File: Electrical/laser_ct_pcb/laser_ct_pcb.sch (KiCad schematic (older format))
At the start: 3 parts

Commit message: End of E07.
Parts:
- added Q? (x9): Q_Photo_NPN, symbol Device:Q_Photo_NPN
- added R? (x9): 1 kOhm, symbol Device:R_US
- added U? (x2): MCP3008, symbol Analog_ADC:MCP3008
- R?: value 10 kOhm -> 1 kOhm
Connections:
- net +5V: now also A?.27 (+5V), R?.1, R?.1, R?.1, R?.1, R?.1, R?.1, R?.1, R?.1, R?.1, U?.15 (Vref), U?.15 (Vref), U?.16 (Vdd), U?.16 (Vdd)
- net GND: now also A?.29 (GND), A?.4 (GND), Q?.2 (E), Q?.2 (E), Q?.2 (E), Q?.2 (E), Q?.2 (E), Q?.2 (E), Q?.2 (E), Q?.2 (E), Q?.2 (E), U?.14 (AGND), U?.14 (AGND), U?.9 (DGND), U?.9 (DGND)
- net at A?.12 (D9): now also U?.10 (~CS~/SHDN)
- net at A?.13 (D10): now also U?.10 (~CS~/SHDN)
- net at A?.14 (D11): now also U?.11 (Din), U?.11 (Din)
- net at A?.15 (D12): now also U?.12 (Dout), U?.12 (Dout)
- net at A?.16 (D13): now also U?.13 (CLK), U?.13 (CLK)
- new net: Q?.1 (C), R?.2 (x9)
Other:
- moved on the sheet: A?, Q?, R?

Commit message: End of Episode 08.
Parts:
- removed Q? (x10): Q_Photo_NPN, symbol Device:Q_Photo_NPN
- removed R? (x10): 1 kOhm, symbol Device:R_US

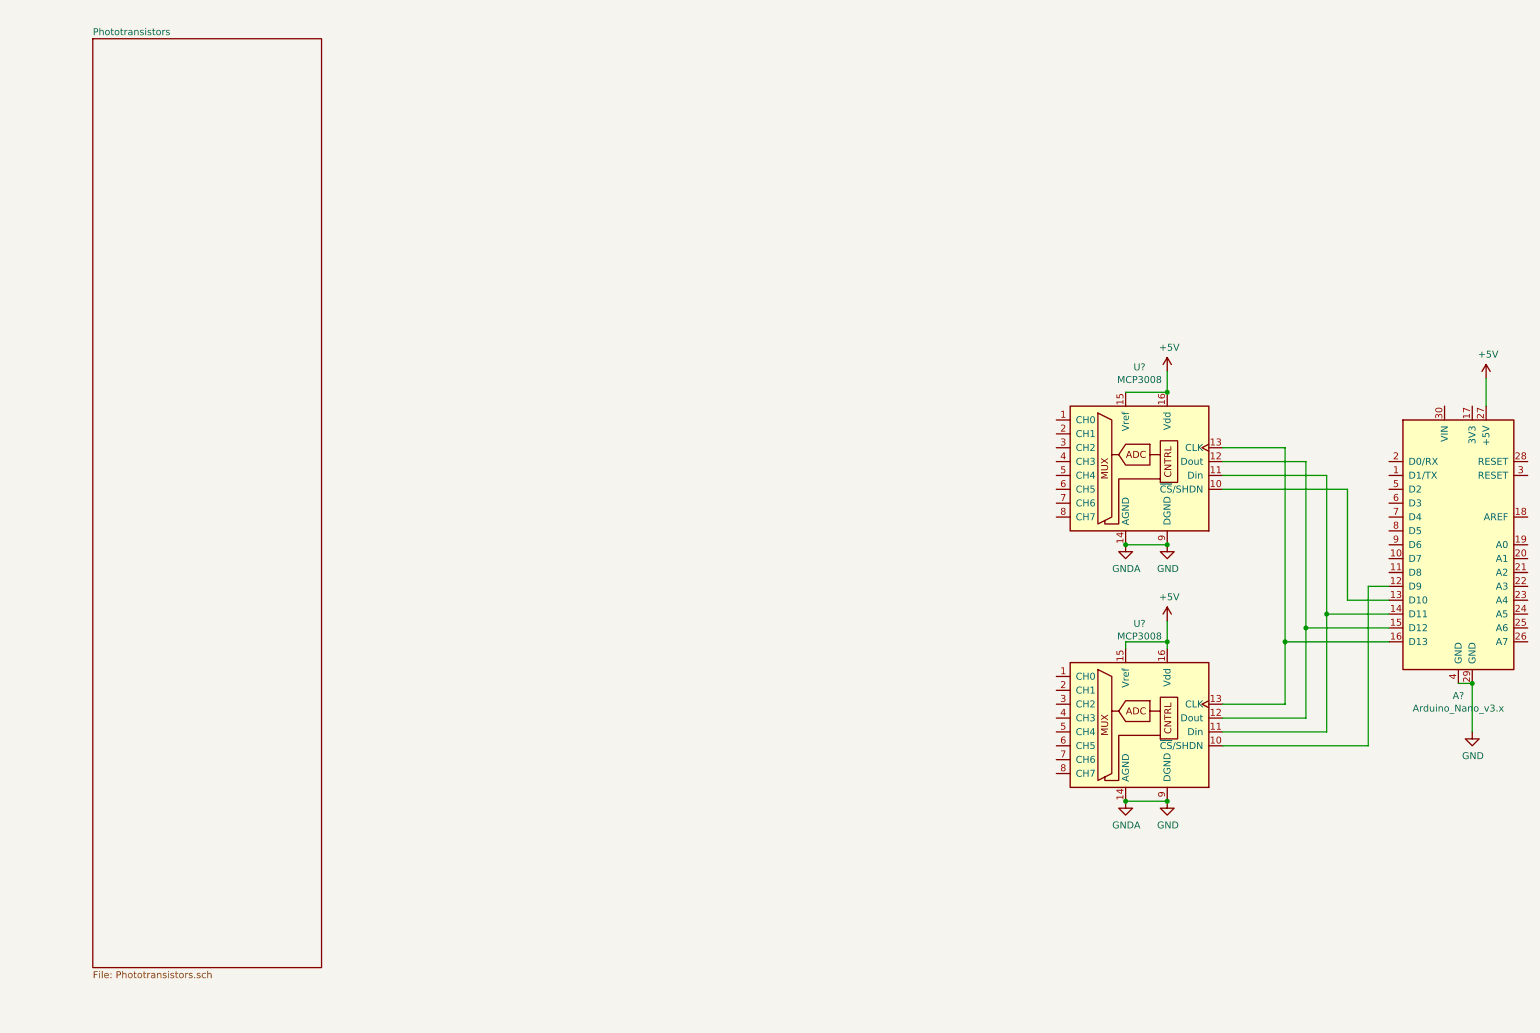
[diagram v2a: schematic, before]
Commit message: Fixed through hole size on ICSP board.
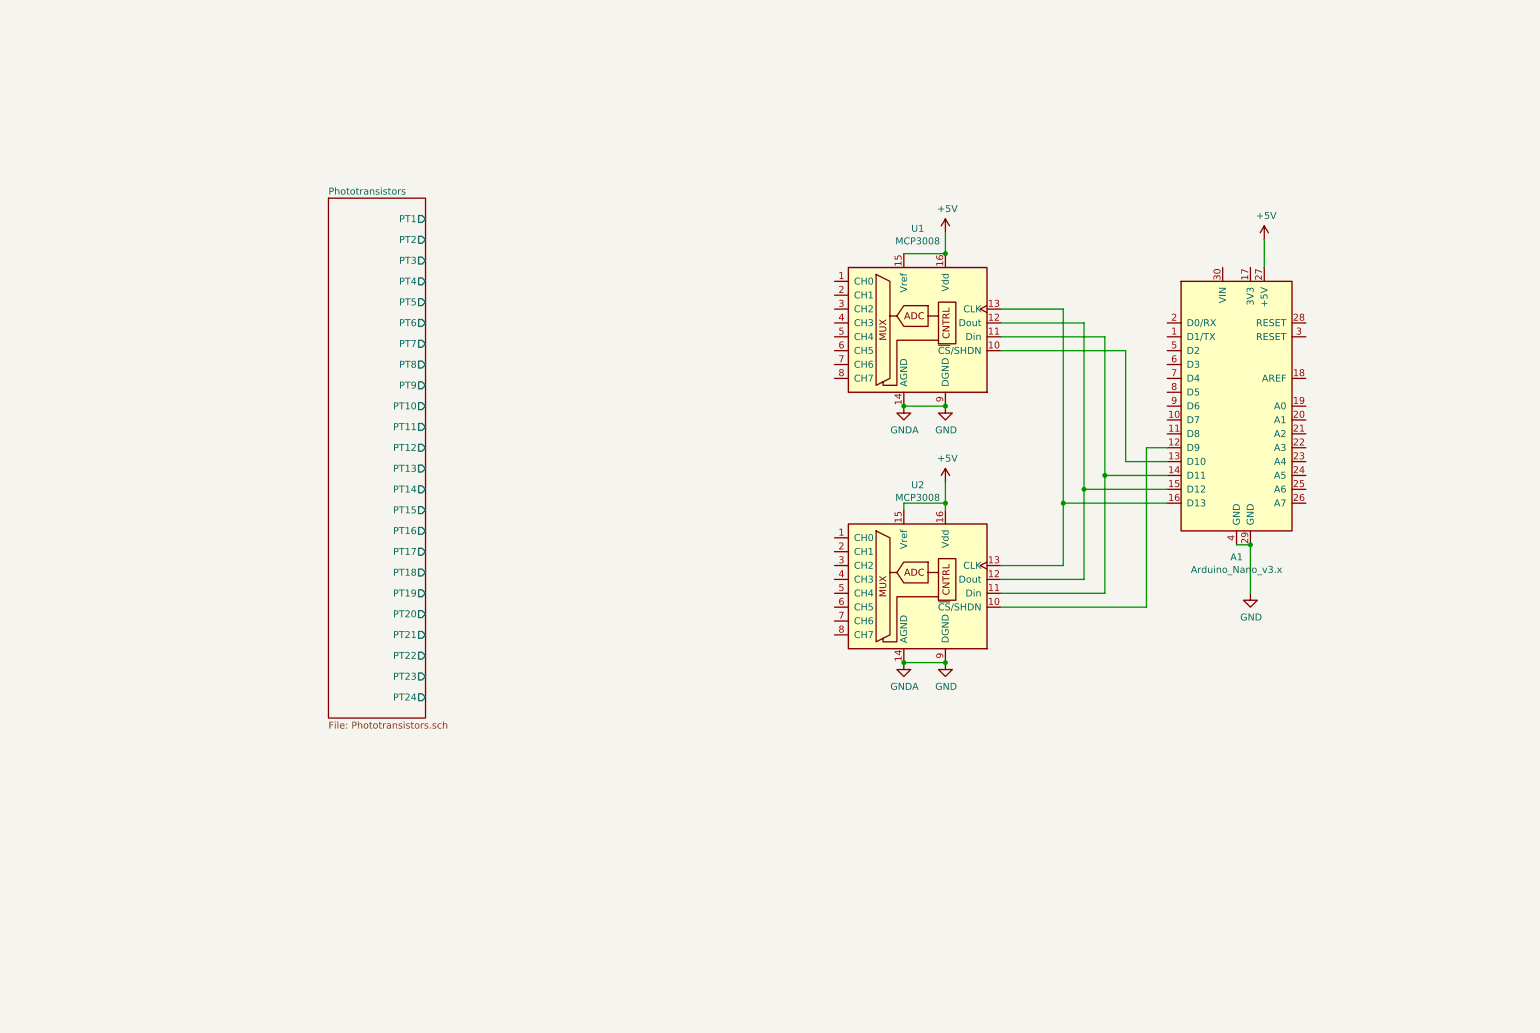
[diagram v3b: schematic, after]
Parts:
- U1, U2: renamed from U?; footprint (none) -> Package_DIP:DIP-16_W7.62mm
- gave numbers to parts that had none: 1
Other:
- moved on the sheet: A1, U1, U2

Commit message: End of episode 09.
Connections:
- net Phototransistors/PT1: now also U1.8 (CH7)
- net Phototransistors/PT17: now also A1.26 (A7)
- net Phototransistors/PT18: now also A1.25 (A6)
- net Phototransistors/PT19: now also A1.24 (A5)
- net Phototransistors/PT20: now also A1.23 (A4)
- net Phototransistors/PT21: now also A1.22 (A3)
- net Phototransistors/PT22: now also A1.21 (A2)
- net Phototransistors/PT23: now also A1.20 (A1)
- net Phototransistors/PT24: now also A1.19 (A0)
- net Phototransistors/PT9: now also U2.8 (CH7)
- net PT8: now reaches U1.1 (CH0)
- net PT7: now reaches U1.2 (CH1)
- net PT6: now reaches U1.3 (CH2)
- net PT5: now reaches U1.4 (CH3)
- net PT4: now reaches U1.5 (CH4)
- net PT3: now reaches U1.6 (CH5)
- net PT2: now reaches U1.7 (CH6)
- net PT16: now reaches U2.1 (CH0)
- net PT15: now reaches U2.2 (CH1)
- net PT14: now reaches U2.3 (CH2)
- net PT13: now reaches U2.4 (CH3)
- net PT12: now reaches U2.5 (CH4)
- net PT11: now reaches U2.6 (CH5)
- net PT10: now reaches U2.7 (CH6)
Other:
- moved on the sheet: A1, U1, U2

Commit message: End of episode 09.
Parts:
- added C1: 0.1uF, Capacitor_THT:CP_Radial_D5.0mm_P2.50mm, symbol Device:CP
- added C2: 10uF, Capacitor_THT:CP_Radial_D5.0mm_P2.50mm, symbol Device:CP
- added J1: Barrel_Jack_Switch, Connector_BarrelJack:BarrelJack_Horizontal, symbol Connector:Barrel_Jack_Switch
- added U3: MIC29310-5.0WT, Package_TO_SOT_THT:TO-220-3_Horizontal_TabDown, symbol Regulator_Linear:L7805
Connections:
- net labels added: +VDC
- wire segments 108 -> 121
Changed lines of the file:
@@
 Text Label 2050 3500 0    50   ~ 0
 PT16
+$Comp
+L Regulator_Linear:L7805 U3
+U 1 1 5D77A12E
+P 1700 7050
+F 0 "U3" H 1700 7292 50  0000 C CNN
+F 1 "MIC29310-5.0WT" H 1700 7201 50  0000 C CNN
+F 2 "Package_TO_SOT_THT:TO-220-3_Horizontal_TabDown" H 1725 6900 50  0001 L CIN
+F 3 "http://www.st.com/content/ccc/resource/technical/document/datasheet/41/4f/b3/b0/12/d4/47/88/CD00000444.pdf/files/CD00000444.pdf/jcr:content/translations/en.CD00000444.pdf" H 1700 7000 50  0001 C CNN
+	1    1700 7050
+	1    0    0    -1
+$EndComp
+$Comp
+L Device:CP C2
+U 1 1 5D77BA9C
+P 2300 7250
+F 0 "C2" H 2418 7296 50  0000 L CNN
+F 1 "10uF" H 2418 7205 50  0000 L CNN
+F 2 "Capacitor_THT:CP_Radial_D5.0mm_P2.50mm" H 2338 7100 50  0001 C CNN
+F 3 "~" H 2300 7250 50  0001 C CNN
+	1    2300 7250
+	1    0    0    -1
+$EndComp
+Wire Wire Line
+	2300 7100 2300 7050
+Wire Wire Line
+	2300 7050 2000 7050
+$Comp
+L Device:CP C1
+U 1 1 5D7807CE
+P 1000 7250
+F 0 "C1" H 1118 7296 50  0000 L CNN
+F 1 "0.1uF" H 1118 7205 50  0000 L CNN
+F 2 "Capacitor_THT:CP_Radial_D5.0mm_P2.50mm" H 1038 7100 50  0001 C CNN
+F 3 "~" H 1000 7250 50  0001 C CNN
+	1    1000 7250
+	1    0    0    -1
+$EndComp
+Wire Wire Line
+	1000 7050 1400 7050
+Wire Wire Line
+	1000 7100 1000 7050
+$Comp
+L power:GND #PWR0157
+U 1 1 5D78EE36
+P 1700 7500
+F 0 "#PWR0157" H 1700 7250 50  0001 C CNN
+F 1 "GND" H 1705 7327 50  0000 C CNN
+F 2 "" H 1700 7500 50  0001 C CNN
+F 3 "" H 1700 7500 50  0001 C CNN
+	1    1700 7500
+	1    0    0    -1
+$EndComp
+Wire Wire Line
+	1700 7350 1700 7400
+Wire Wire Line
+	2300 7400 1700 7400
+Connection ~ 1700 7400
+Wire Wire Line
+	1700 7400 1700 7500
+Wire Wire Line
+	1000 7400 1700 7400
+Wire Wire Line
+	2650 7050 2300 7050
+Connection ~ 2300 7050
+$Comp
+L power:+5V #PWR0158
+U 1 1 5D7ABF35
+P 2650 7050
+F 0 "#PWR0158" H 2650 6900 50  0001 C CNN
+F 1 "+5V" H 2665 7223 50  0000 C CNN
+F 2 "" H 2650 7050 50  0001 C CNN
+F 3 "" H 2650 7050 50  0001 C CNN
+	1    2650 7050
+	1    0    0    -1
+$EndComp
+$Comp
+L power:+VDC #PWR0159
+U 1 1 5D7ACBAD
+P 800 7050
+F 0 "#PWR0159" H 800 6950 50  0001 C CNN
+F 1 "+VDC" H 800 7325 50  0000 C CNN
+F 2 "" H 800 7050 50  0001 C CNN
+F 3 "" H 800 7050 50  0001 C CNN
+	1    800  7050
+	1    0    0    -1
+$EndComp
+Wire Wire Line
+	1000 7050 800  7050
+Connection ~ 1000 7050
+$Comp
+L Connector:Barrel_Jack_Switch J1
+U 1 1 5D7B93FB
+P 3600 7150
+F 0 "J1" H 3657 7467 50  0000 C CNN
+F 1 "Barrel_Jack_Switch" H 3657 7376 50  0000 C CNN
+F 2 "Connector_BarrelJack:BarrelJack_Horizontal" H 3650 7110 50  0001 C CNN
+F 3 "~" H 3650 7110 50  0001 C CNN
+	1    3600 7150
+	1    0    0    -1
+$EndComp
+$Comp
+L power:GND #PWR0160
+U 1 1 5D7BB775
+P 4000 7300
+F 0 "#PWR0160" H 4000 7050 50  0001 C CNN
+F 1 "GND" H 4005 7127 50  0000 C CNN
+F 2 "" H 4000 7300 50  0001 C CNN
+F 3 "" H 4000 7300 50  0001 C CNN
+	1    4000 7300
+	1    0    0    -1
+$EndComp
+Wire Wire Line
+	4000 7300 4000 7250
+Wire Wire Line
+	4000 7250 3900 7250
+$Comp
+L power:+VDC #PWR0161
+U 1 1 5D7C0C4F
+P 4150 7050
+F 0 "#PWR0161" H 4150 6950 50  0001 C CNN
+F 1 "+VDC" H 4150 7325 50  0000 C CNN
+F 2 "" H 4150 7050 50  0001 C CNN
+F 3 "" H 4150 7050 50  0001 C CNN
+	1    4150 7050
+	1    0    0    -1
+$EndComp
+Wire Wire Line
+	3900 7050 4150 7050
 $EndSCHEMATC

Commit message: End of episode 10.
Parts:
- added M1: 28BYJ-48, Connector_JST:JST_XH_B5B-XH-AM_1x05_P2.50mm_Vertical, symbol laser_ct:28BYJ-48
- added U4: ULN2003A, Package_DIP:DIP-16_W7.62mm, symbol Transistor_Array:ULN2003A
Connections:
- net labels added: M1, M2, M3, M4
- wire segments 121 -> 158
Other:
- moved on the sheet: A1, U1, U2

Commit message: Added LED indicators for motor coils.
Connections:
- net labels added: A, B, C, D
- wire segments 158 -> 162

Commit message: End of episode 11.
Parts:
- A1: footprint Module:Arduino_Nano -> laser_ct:Arduino_Nano
- J1: footprint Connector_BarrelJack:BarrelJack_Horizontal -> laser_ct:BarrelJack_Horizontal
- M1: footprint Connector_JST:JST_XH_B5B-XH-AM_1x05_P2.50mm_Vertical -> laser_ct:JST_XH_B5B-XH-AM_1x05_P2.50mm_Vertical
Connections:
- wire segments 162 -> 164
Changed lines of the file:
@@
 F 0 "A1" H 8100 1061 50  0000 C CNN
 F 1 "Arduino_Nano_v3.x" H 8100 970 50  0000 C CNN
-F 2 "Module:Arduino_Nano" H 8250 1200 50  0001 L CNN
+F 2 "laser_ct:Arduino_Nano" H 8250 1200 50  0001 L CNN
 F 3 "http://www.mouser.com/pdfdocs/Gravitech_Arduino_Nano3_0.pdf" H 8100 1150 50  0001 C CNN
 	1    8100 2150
@@
 L power:+5V #PWR0101
 U 1 1 5D55D0A0
-P 8300 950
-F 0 "#PWR0101" H 8300 800 50  0001 C CNN
-F 1 "+5V" H 8315 1123 50  0000 C CNN
-F 2 "" H 8300 950 50  0001 C CNN
-F 3 "" H 8300 950 50  0001 C CNN
-	1    8300 950
-	1    0    0    -1
-$EndComp
-Wire Wire Line
-	8300 1150 8300 950
+P 8000 950
+F 0 "#PWR0101" H 8000 800 50  0001 C CNN
+F 1 "+5V" H 8015 1123 50  0000 C CNN
+F 2 "" H 8000 950 50  0001 C CNN
+F 3 "" H 8000 950 50  0001 C CNN
+	1    8000 950
+	1    0    0    -1
+$EndComp
+Wire Wire Line
+	8000 1150 8000 950
 $Comp
 L power:+5V #PWR0102
@@
 F 0 "M1" H 5138 6974 50  0000 L CNN
 F 1 "28BYJ-48" H 5138 6883 50  0000 L CNN
-F 2 "Connector_JST:JST_XH_B5B-XH-AM_1x05_P2.50mm_Vertical" H 4960 6840 50  0001 C CNN
+F 2 "laser_ct:JST_XH_B5B-XH-AM_1x05_P2.50mm_Vertical" H 4960 6840 50  0001 C CNN
 F 3 "http://www.infineon.com/dgdl/Application-Note-TLE8110EE_driving_UniPolarStepperMotor_V1.1.pdf?fileId=db3a30431be39b97011be5d0aa0a00b0" H 4960 6840 50  0001 C CNN
 	1    4950 6850
@@
 F 0 "J1" H 1057 6367 50  0000 C CNN
 F 1 "Barrel_Jack_Switch" H 1057 6276 50  0000 C CNN
-F 2 "Connector_BarrelJack:BarrelJack_Horizontal" H 1050 6010 50  0001 C CNN
+F 2 "laser_ct:BarrelJack_Horizontal" H 1050 6010 50  0001 C CNN
 F 3 "~" H 1050 6010 50  0001 C CNN
 	1    1000 6050
@@
 Text Label 6000 7100 2    50   ~ 0
 D
+Wire Wire Line
+	1300 6050 1400 6050
+Wire Wire Line
+	1400 6050 1400 6150
+Connection ~ 1400 6150
 $EndSCHEMATC
